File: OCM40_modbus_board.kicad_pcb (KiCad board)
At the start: 2 copper layers, 20.4 x 18.8 mm, 26 parts, among them J1 Conn_01x08, J2 Conn_01x08, J3 Conn_02x03_Odd_Even, U1 AP2204K-5.0, U2 SN65LBC176D, U3 ATMEGA328PB-AU, U4 SN65LBC176D, Y2 Crystal_GND2

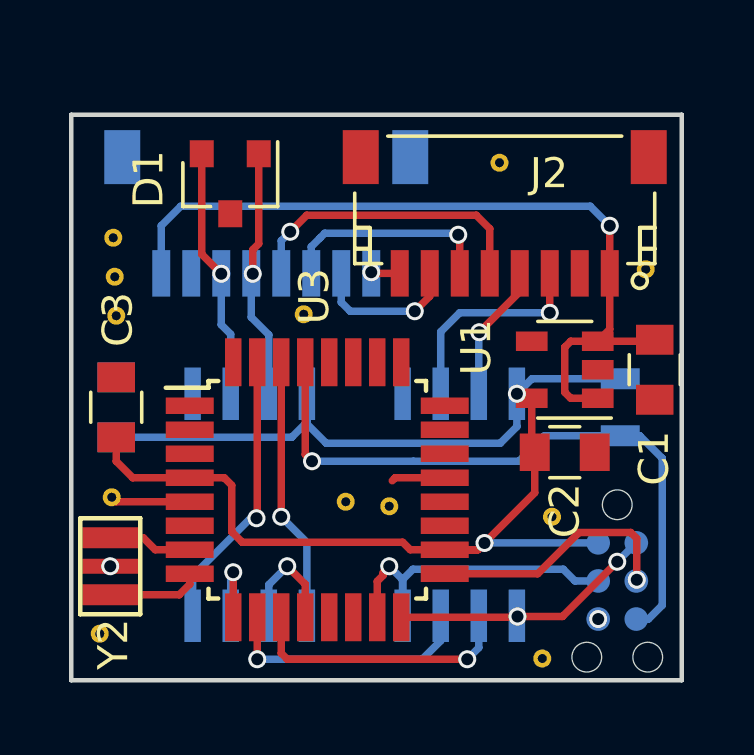
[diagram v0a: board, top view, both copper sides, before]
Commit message: --REV1-- Change connector J1 & J2 footprint. Changes J2 connection mirroed. Change U2 & U4 footprint to correct size. DONE
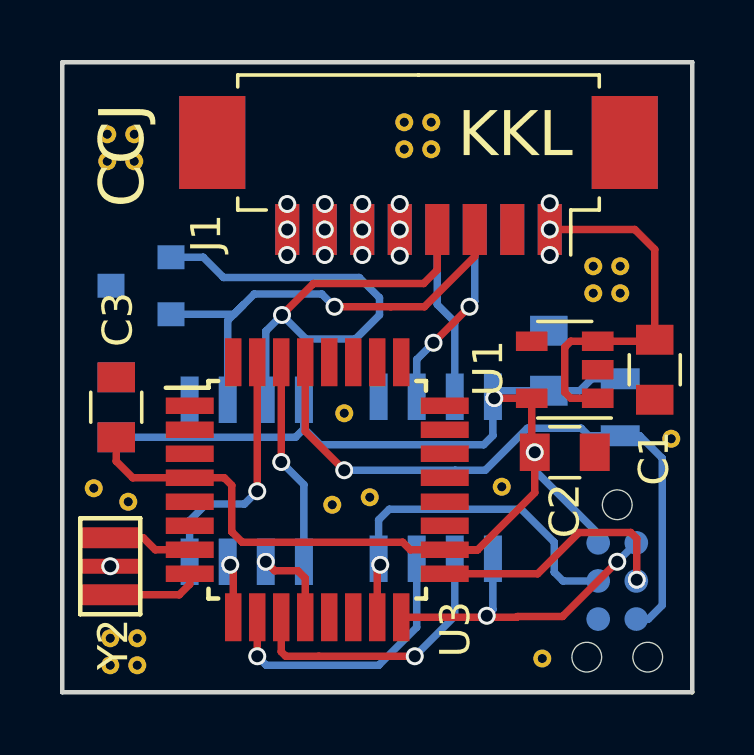
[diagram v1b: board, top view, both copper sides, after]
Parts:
- added C4: 10u, Capacitors_SMD:C_0805, B.Cu at (134.2, 112.0)
- added REF**: via_0.6mm, kenneth:via_0.6mm, F.Cu at (120.5, 122.1)
- added REF**: via_0.6mm, kenneth:via_0.6mm, F.Cu at (119.5, 104.4)
- added REF**: via_0.6mm, kenneth:via_0.6mm, F.Cu at (120.4, 104.4)
- added REF**: via_0.6mm, kenneth:via_0.6mm, F.Cu at (119.5, 105.3)
- added REF**: via_0.6mm, kenneth:via_0.6mm, F.Cu at (119.6, 121.2)
- added REF**: via_0.6mm, kenneth:via_0.6mm, F.Cu at (120.5, 121.2)
- added REF**: via_0.6mm, kenneth:via_0.6mm, F.Cu at (119.6, 122.1)
- added REF**: via_0.6mm, kenneth:via_0.6mm, F.Cu at (136.6, 109.7)
- added REF**: via_0.6mm, kenneth:via_0.6mm, F.Cu at (135.7, 108.8)
- added REF**: via_0.6mm, kenneth:via_0.6mm, F.Cu at (136.6, 108.8)
- added REF**: via_0.6mm, kenneth:via_0.6mm, F.Cu at (135.7, 109.7)
- added REF**: via_0.6mm, kenneth:via_0.6mm, F.Cu at (120.4, 105.3)
- D1: moved to B.Cu
- J1: footprint Connectors_JST:JST_SH_SM08B-SRSS-TB_08x1.00mm_Angled -> Connectors_Molex:Molex_PicoBlade_53261-0871_08x1.25mm_Angled; moved to F.Cu
- J2: footprint Connectors_JST:JST_SH_SM08B-SRSS-TB_08x1.00mm_Angled -> Connectors_Molex:Molex_PicoBlade_53261-0871_08x1.25mm_Angled; moved to B.Cu
- U2, U4: footprint Housings_SOIC:SO-8_5.3x6.2mm_Pitch1.27mm -> Housings_SOIC:SOIC-8_3.9x4.9mm_Pitch1.27mm
- moved REF** 14.7 mm to (132.7, 116.2)
- moved REF** 11.0 mm to (130.3, 104.9)
- moved REF** 11.0 mm to (127.4, 113.7)
- moved REF** 8.99 mm to (129.4, 104.9)
- moved REF** 7.22 mm to (129.4, 104.0)
- moved REF** 6.21 mm to (120.2, 116.7)
- moved J1 5.17 mm to (129.9, 106.1), turned to 180 degrees
- moved REF** 4.75 mm to (138.3, 114.5)
- moved D1 4.52 mm to (120.6, 109.5), turned to 180 degrees
- moved J2 3.04 mm to (129.9, 106.1), turned to 0 degrees
- moved REF** 2.65 mm to (130.3, 104.0)
- moved REF** 1.90 mm to (127.0, 116.8)
- moved U4 1.20 mm to (130.4, 115.8)
- moved REF** 0.81 mm to (128.2, 116.5)
- moved U2 0.81 mm to (124.2, 116.0)
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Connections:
- J2 pad 1: +24V -> /RS-422-Y
- J2 pad 2: GND -> /RS-422-Z
- J2 pad 3: Net-(J2-Pad3) -> /RS-422-B
- J2 pad 4: Net-(J2-Pad4) -> /RS-422-A
- J2 pad 5: /RS-422-A -> Net-(J2-Pad5)
- J2 pad 6: /RS-422-B -> Net-(J2-Pad6)
- J2 pad 7: /RS-422-Z -> GND
- J2 pad 8: /RS-422-Y -> +24V
- U4 pad 6: Net-(J2-Pad3) -> Net-(J2-Pad6)
- U4 pad 7: Net-(J2-Pad4) -> Net-(J2-Pad5)
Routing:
- net Net-(D1-Pad1): track 8.39 -> 22.2 mm
- net +24V: track 26.9 -> 14.3 mm, vias 1 -> 3
- net /RS-422-A: track 10.1 -> 2.58 mm, vias 1 -> 3
- net Net-(J2-Pad3): track 7.28 -> 0.00 mm, vias 1 -> 0
- net Net-(D1-Pad2): track 8.42 -> 15.5 mm
- net Net-(J2-Pad6): track 0.00 -> 6.38 mm, vias 0 -> 2
- net Net-(J2-Pad5): track 0.00 -> 5.82 mm
- net /RS-422-B: track 7.30 -> 2.55 mm, vias 1 -> 3
- net Net-(J2-Pad4): track 4.58 -> 0.00 mm, vias 1 -> 0
- net GND: track 4.47 -> 0.00 mm, vias 2 -> 1
- net /RS-422-Z: track 5.01 -> 1.70 mm, vias 1 -> 3
- net /RX1/MISO: track 8.90 -> 11.0 mm
- net /RX0: track 8.80 -> 6.96 mm
- net /TX0: track 9.46 -> 8.33 mm
- net /PD4: track 2.99 -> 1.93 mm
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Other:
- board size 20.4 x 18.8 mm -> 21 x 21 mm
- board text added: "CCJ"
